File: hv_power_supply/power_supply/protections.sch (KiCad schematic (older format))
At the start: 7 parts, among them J1 MicroFit_RA_R_2, K1 DBR71210(NC), K2 LI12-1A85(NO), Q2 SSM3K333R, SW1 SW_Push_SPST_NO

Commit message: Remove resistor
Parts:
- removed J1: MicroFit_RA_R_2, footprints:MicroFit_RA_2, symbol formula:MicroFit_RA_R_2
- removed R2: R_100K, footprints:R_0805_OEM, symbol formula:R_100K
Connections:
- net labels removed: ACH+, ACH-
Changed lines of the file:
@@
 Wire Notes Line
 	3000 800  3000 2400
-$Comp
-L formula:MicroFit_RA_R_2 J1
-U 1 1 5FC7105C
-P 6400 1150
-F 0 "J1" H 6458 1425 50  0000 C CNN
-F 1 "MicroFit_RA_R_2" H 6458 1334 50  0000 C CNN
-F 2 "footprints:MicroFit_RA_2" H 6350 1350 50  0001 C CNN
-F 3 "https://www.molex.com/pdm_docs/sd/436500201_sd.pdf" H 6350 1350 50  0001 C CNN
-F 4 "DK" H 6500 1400 50  0001 C CNN "MFN"
-F 5 "WM1865-ND" H 6600 1500 50  0001 C CNN "MPN"
-F 6 "https://www.digikey.com/product-detail/en/molex/0436500201/WM1865-ND/268994" H 6400 1300 50  0001 C CNN "PurchasingLink"
-	1    6400 1150
-	1    0    0    -1
-$EndComp
-Text HLabel 6650 1100 2    47   Input ~ 0
-ACH+
-Text HLabel 6650 1200 2    47   Output ~ 0
-ACH-
 Wire Wire Line
 	800  1550 1300 1550
@@
 Wire Notes Line
 	600  2400 2650 2400
-$Comp
-L formula:R_100K R2
-U 1 1 5FC80149
-P 2050 1900
-F 0 "R2" H 2120 1946 50  0000 L CNN
-F 1 "R_100K" H 2120 1855 50  0000 L CNN
-F 2 "footprints:R_0805_OEM" H 1980 1900 50  0001 C CNN
-F 3 "https://industrial.panasonic.com/cdbs/www-data/pdf/RDA0000/AOA0000C304.pdf" H 2130 1900 50  0001 C CNN
-F 4 "DK" H 2050 1900 60  0001 C CNN "MFN"
-F 5 "P100KCCT-ND" H 2050 1900 60  0001 C CNN "MPN"
-F 6 "https://www.digikey.com/product-detail/en/panasonic-electronic-components/ERJ-6ENF1003V/P100KCCT-ND/119551" H 2530 2300 60  0001 C CNN "PurchasingLink"
-	1    2050 1900
-	1    0    0    -1
-$EndComp
 $EndSCHEMATC

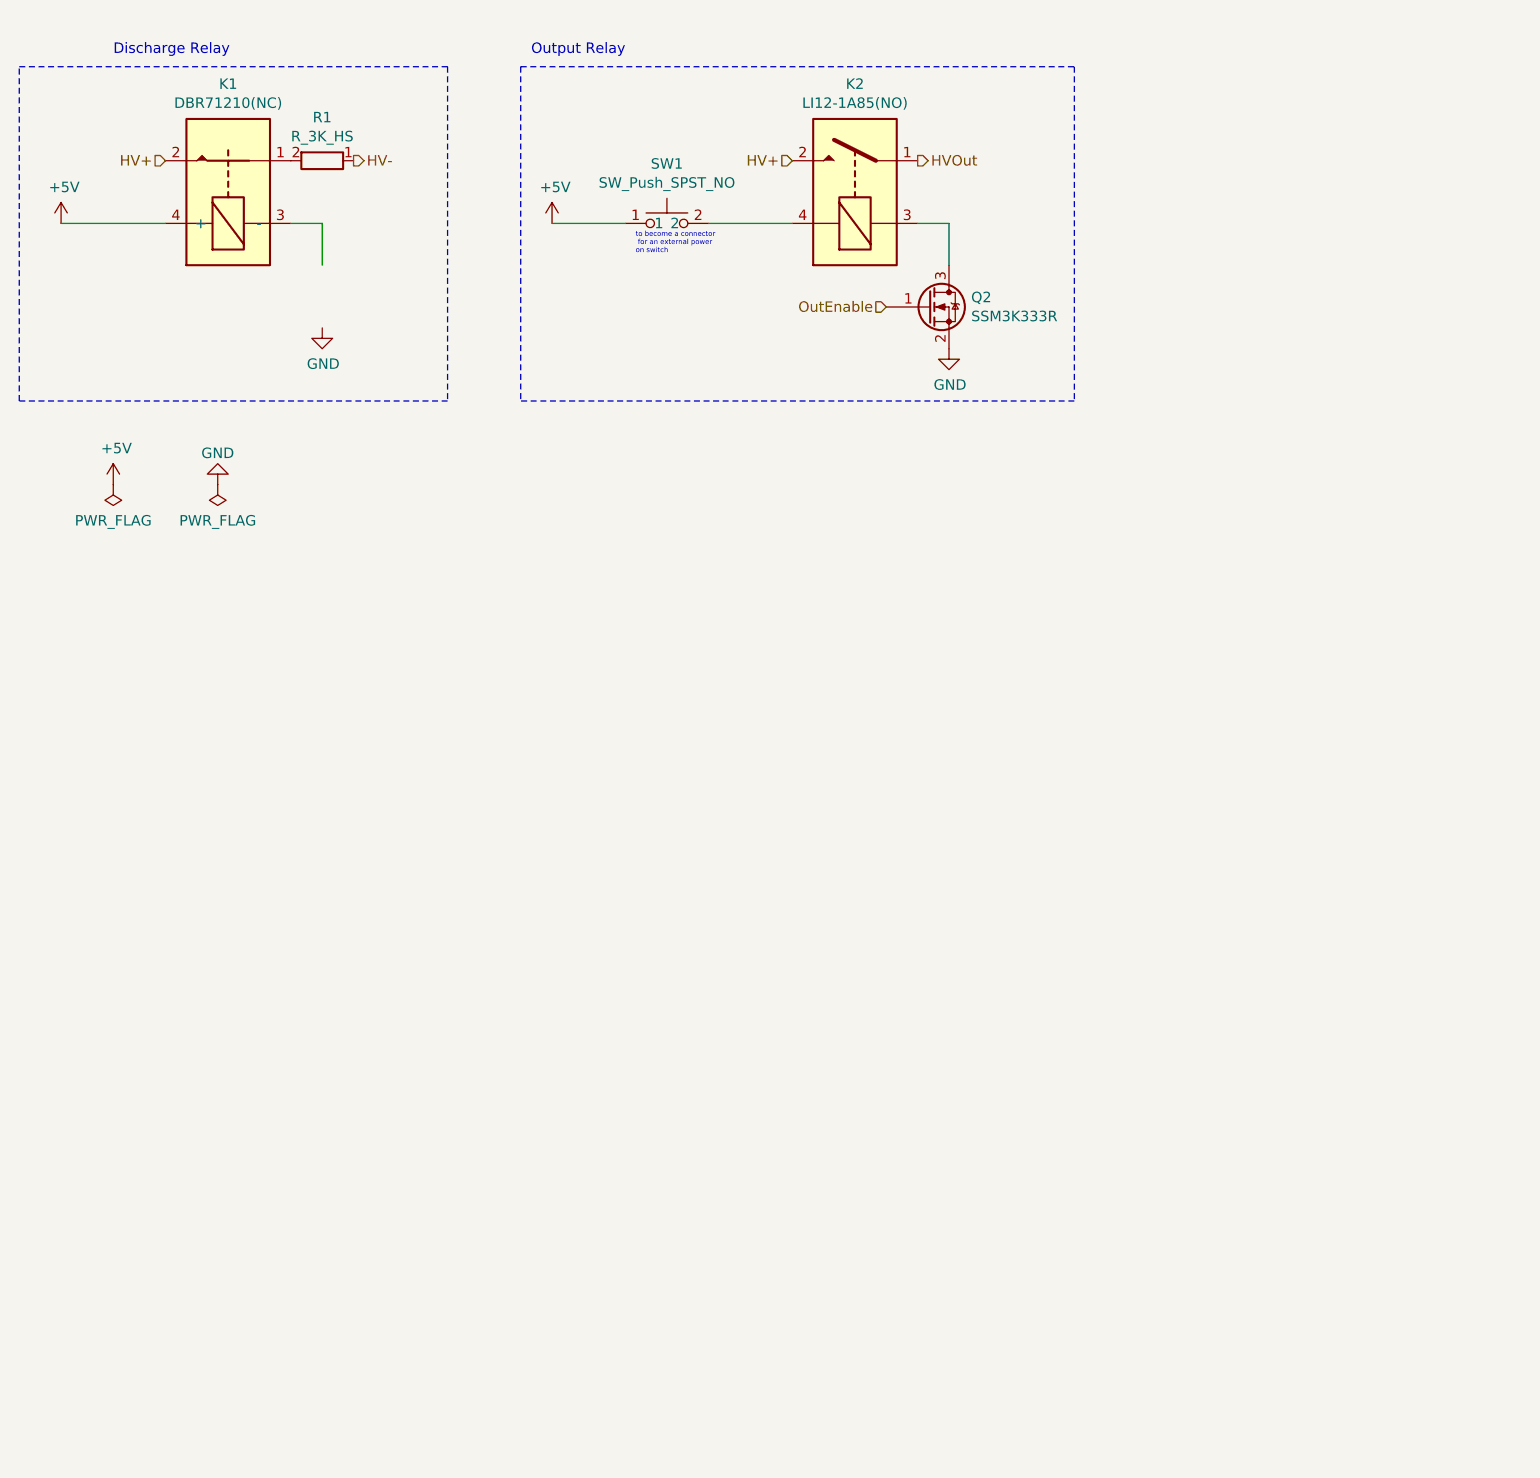
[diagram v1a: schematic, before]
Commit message: Add suppression diodes
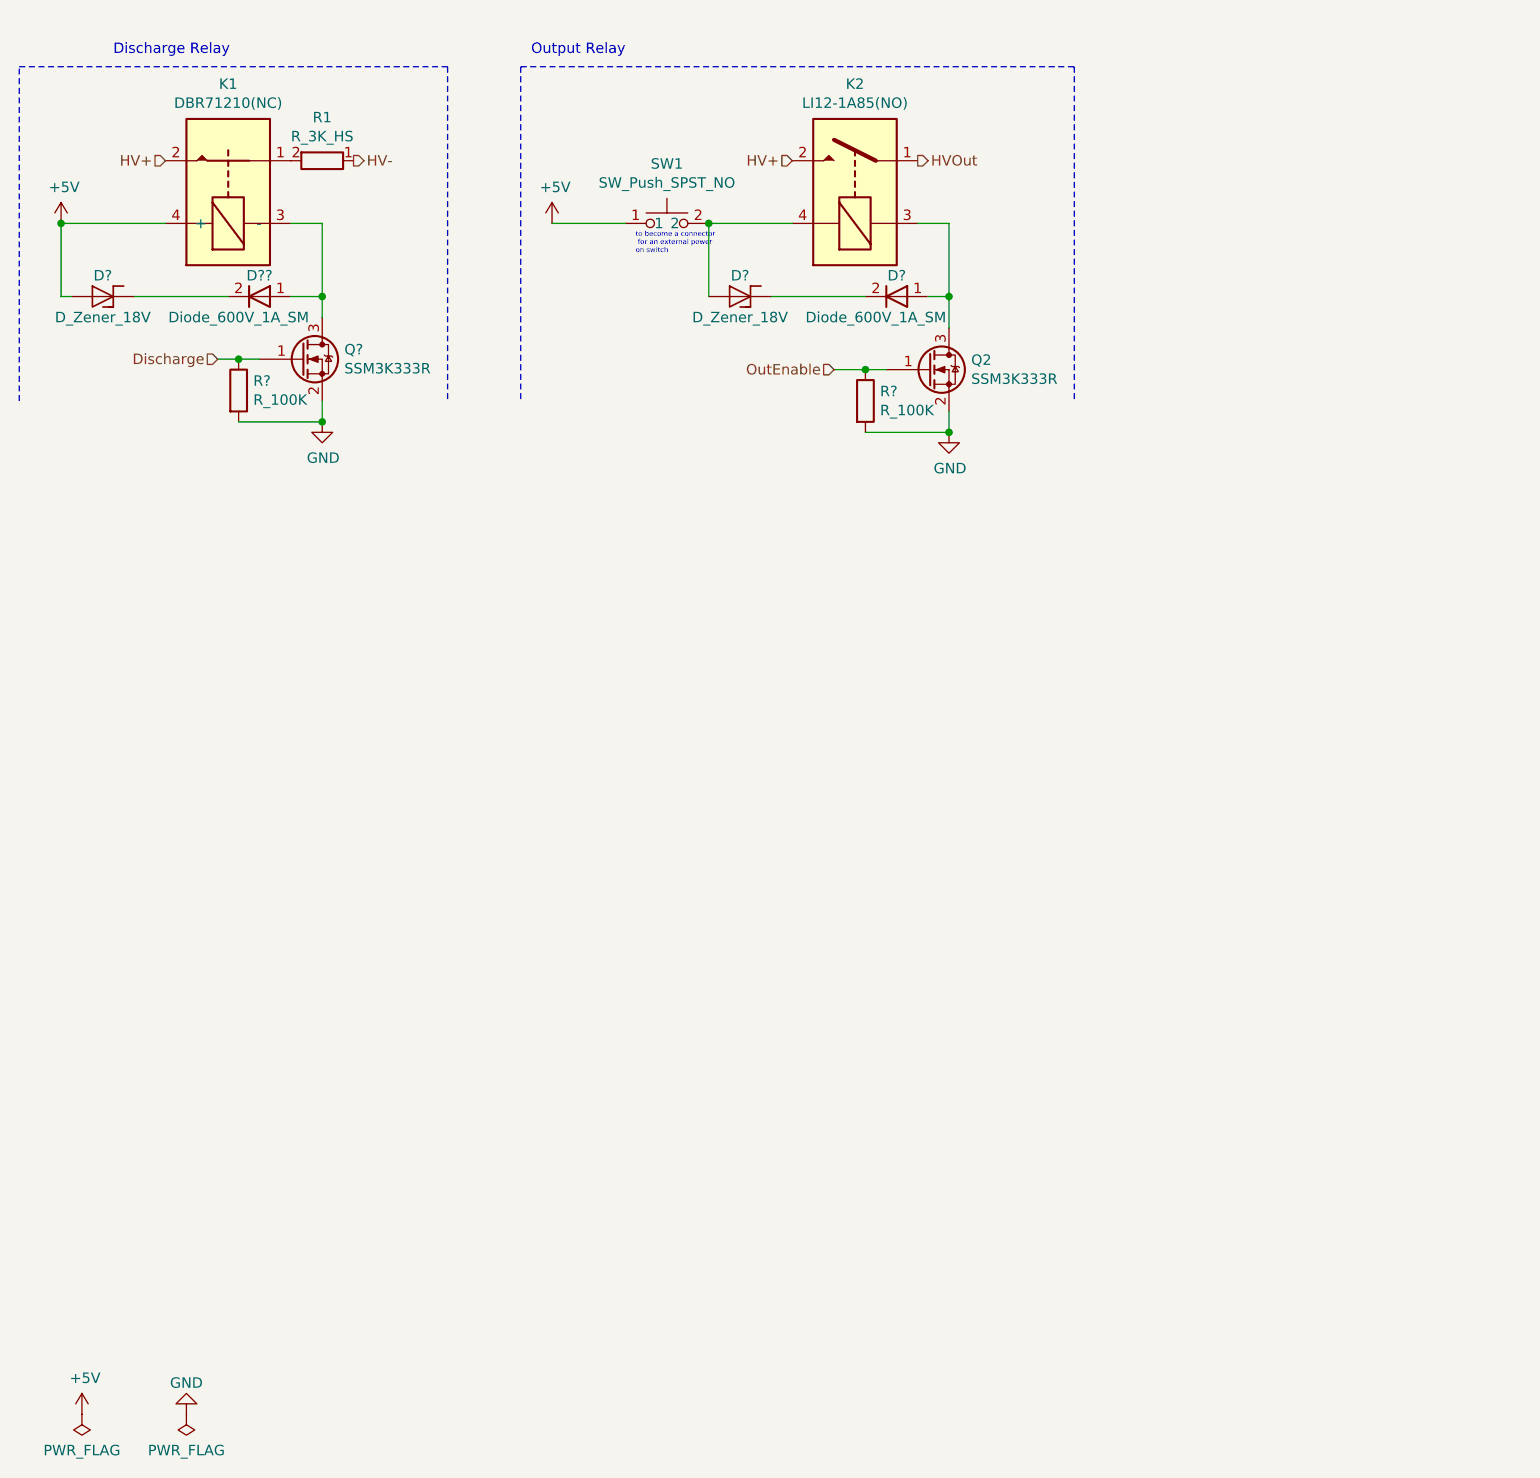
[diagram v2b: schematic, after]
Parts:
- added D? (x2): D_Zener_18V, footprints:DO-214AA, symbol formula:D_Zener_18V
- added D?, D??: Diode_600V_1A_SM, footprints:Diode_600V_1A_SM, symbol formula:Diode_600V_1A_SM
- added Q?: SSM3K333R, footprints:SOT-23F, symbol formula:SSM3K333R
- added R? (x2): R_100K, footprints:R_0805_OEM, symbol formula:R_100K
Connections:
- net labels added: Discharge
- wire segments 7 -> 24
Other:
- moved on the sheet: Q2
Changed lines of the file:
@@
 Wire Wire Line
 	1900 1550 2050 1550
-Wire Wire Line
-	2050 1550 2050 1750
 $Comp
 L power:GND #PWR04
 U 1 1 5FC34A9E
-P 2050 2050
-F 0 "#PWR04" H 2050 1800 50  0001 C CNN
-F 1 "GND" H 2055 1877 50  0000 C CNN
-F 2 "" H 2050 2050 50  0001 C CNN
-F 3 "" H 2050 2050 50  0001 C CNN
-	1    2050 2050
+P 2050 2500
+F 0 "#PWR04" H 2050 2250 50  0001 C CNN
+F 1 "GND" H 2055 2327 50  0000 C CNN
+F 2 "" H 2050 2500 50  0001 C CNN
+F 3 "" H 2050 2500 50  0001 C CNN
+	1    2050 2500
 	1    0    0    -1
 $EndComp
@@
 L power:+5V #PWR01
 U 1 1 5FC37E55
-P 1050 2800
-F 0 "#PWR01" H 1050 2650 50  0001 C CNN
-F 1 "+5V" H 1065 2973 50  0000 C CNN
-F 2 "" H 1050 2800 50  0001 C CNN
-F 3 "" H 1050 2800 50  0001 C CNN
-	1    1050 2800
+P 900 7250
+F 0 "#PWR01" H 900 7100 50  0001 C CNN
+F 1 "+5V" H 915 7423 50  0000 C CNN
+F 2 "" H 900 7250 50  0001 C CNN
+F 3 "" H 900 7250 50  0001 C CNN
+	1    900  7250
 	1    0    0    -1
 $EndComp
@@
 L power:PWR_FLAG #FLG01
 U 1 1 5FC38367
-P 1050 2800
-F 0 "#FLG01" H 1050 2875 50  0001 C CNN
-F 1 "PWR_FLAG" H 1050 2973 50  0000 C CNN
-F 2 "" H 1050 2800 50  0001 C CNN
-F 3 "~" H 1050 2800 50  0001 C CNN
-	1    1050 2800
+P 900 7250
+F 0 "#FLG01" H 900 7325 50  0001 C CNN
+F 1 "PWR_FLAG" H 900 7423 50  0000 C CNN
+F 2 "" H 900 7250 50  0001 C CNN
+F 3 "~" H 900 7250 50  0001 C CNN
+	1    900  7250
 	-1   0    0    1
 $EndComp
@@
 L power:PWR_FLAG #FLG02
 U 1 1 5FC38703
-P 1550 2800
-F 0 "#FLG02" H 1550 2875 50  0001 C CNN
-F 1 "PWR_FLAG" H 1550 2973 50  0000 C CNN
-F 2 "" H 1550 2800 50  0001 C CNN
-F 3 "~" H 1550 2800 50  0001 C CNN
-	1    1550 2800
+P 1400 7250
+F 0 "#FLG02" H 1400 7325 50  0001 C CNN
+F 1 "PWR_FLAG" H 1400 7423 50  0000 C CNN
+F 2 "" H 1400 7250 50  0001 C CNN
+F 3 "~" H 1400 7250 50  0001 C CNN
+	1    1400 7250
 	-1   0    0    1
 $EndComp
@@
 L power:GND #PWR02
 U 1 1 5FC38C25
-P 1550 2800
-F 0 "#PWR02" H 1550 2550 50  0001 C CNN
-F 1 "GND" H 1550 2650 50  0000 C CNN
-F 2 "" H 1550 2800 50  0001 C CNN
-F 3 "" H 1550 2800 50  0001 C CNN
-	1    1550 2800
+P 1400 7250
+F 0 "#PWR02" H 1400 7000 50  0001 C CNN
+F 1 "GND" H 1400 7100 50  0000 C CNN
+F 2 "" H 1400 7250 50  0001 C CNN
+F 3 "" H 1400 7250 50  0001 C CNN
+	1    1400 7250
 	-1   0    0    1
 $EndComp
@@
 L formula:SSM3K333R Q2
 U 1 1 5FC3EB17
-P 4950 1950
-F 0 "Q2" H 5156 1996 50  0000 L CNN
-F 1 "SSM3K333R" H 5156 1905 50  0000 L CNN
-F 2 "footprints:SOT-23F" H 5150 1875 50  0001 L CIN
-F 3 "https://drive.google.com/drive/folders/0B-V-iZf33Y4GNzhDQTJZanJRbVk" H 5150 2025 50  0001 L CNN
-F 4 "DK" H 5450 2325 60  0001 C CNN "MFN"
-F 5 "SSM3K333RLFCT-ND" H 5350 2225 60  0001 C CNN "MPN"
-F 6 "https://www.digikey.com/product-detail/en/toshiba-semiconductor-and-storage/SSM3K333RLF/SSM3K333RLFCT-ND/3522391" H 5250 2125 60  0001 C CNN "PurchasingLink"
-	1    4950 1950
+P 4950 2250
+F 0 "Q2" H 5156 2296 50  0000 L CNN
+F 1 "SSM3K333R" H 5156 2205 50  0000 L CNN
+F 2 "footprints:SOT-23F" H 5150 2175 50  0001 L CIN
+F 3 "https://drive.google.com/drive/folders/0B-V-iZf33Y4GNzhDQTJZanJRbVk" H 5150 2325 50  0001 L CNN
+F 4 "DK" H 5450 2625 60  0001 C CNN "MFN"
+F 5 "SSM3K333RLFCT-ND" H 5350 2525 60  0001 C CNN "MPN"
+F 6 "https://www.digikey.com/product-detail/en/toshiba-semiconductor-and-storage/SSM3K333RLF/SSM3K333RLFCT-ND/3522391" H 5250 2425 60  0001 C CNN "PurchasingLink"
+	1    4950 2250
 	1    0    0    -1
 $EndComp
@@
 	1    0    0    -1
 $EndComp
-Text HLabel 4750 1950 0    50   Input ~ 0
+Text HLabel 4500 2250 0    50   Input ~ 0
 OutEnable
 $Comp
@@
 HV+
 Wire Wire Line
-	5050 1750 5050 1550
-Wire Wire Line
 	5050 1550 4900 1550
 $Comp
 L power:GND #PWR06
 U 1 1 5FC4F4BB
-P 5050 2150
-F 0 "#PWR06" H 5050 1900 50  0001 C CNN
-F 1 "GND" H 5055 1977 50  0000 C CNN
-F 2 "" H 5050 2150 50  0001 C CNN
-F 3 "" H 5050 2150 50  0001 C CNN
-	1    5050 2150
+P 5050 2550
+F 0 "#PWR06" H 5050 2300 50  0001 C CNN
+F 1 "GND" H 5055 2377 50  0000 C CNN
+F 2 "" H 5050 2550 50  0001 C CNN
+F 3 "" H 5050 2550 50  0001 C CNN
+	1    5050 2550
 	1    0    0    -1
 $EndComp
@@
 Wire Notes Line
 	3000 800  5650 800
-Wire Notes Line
-	5650 2400 3000 2400
 Text Notes 3050 750  0    50   ~ 0
 Output Relay
@@
 Wire Notes Line
 	600  800  2650 800
-Wire Notes Line
-	600  2400 2650 2400
+$Comp
+L formula:Diode_600V_1A_SM D??
+U 1 1 5FC85209
+P 1750 1900
+F 0 "D??" H 1750 1800 50  0000 C CNN
+F 1 "Diode_600V_1A_SM" H 1850 2000 50  0000 C CNN
+F 2 "footprints:Diode_600V_1A_SM" H 1700 2050 50  0001 C CNN
+F 3 "https://www.st.com/content/ccc/resource/technical/document/datasheet/c7/d5/fe/c4/56/21/41/02/CD00005135.pdf/files/CD00005135.pdf/jcr:content/translations/en.CD00005135.pdf" H 1700 2050 50  0001 C CNN
+F 4 "https://www.digikey.com/product-detail/en/stmicroelectronics/STTH1R06A/497-3765-1-ND/691935" H 1750 2100 50  0001 C CNN "Purchasing Link"
+	1    1750 1900
+	-1   0    0    1
+$EndComp
+$Comp
+L formula:D_Zener_18V D?
+U 1 1 5FC870AF
+P 1000 1900
+F 0 "D?" H 1000 1800 50  0000 C CNN
+F 1 "D_Zener_18V" H 1000 2000 50  0000 C CNN
+F 2 "footprints:DO-214AA" H 900 1900 50  0001 C CNN
+F 3 "http://www.mccsemi.com/up_pdf/SMBJ5338B-SMBJ5388B(SMB).pdf" H 1000 2000 50  0001 C CNN
+F 4 "DK" H 1200 2200 60  0001 C CNN "MFN"
+F 5 "SMBJ5355B-TPMSCT-ND" H 1100 2100 60  0001 C CNN "MPN"
+F 6 "https://www.digikey.com/products/en?keywords=SMBJ5355B-TPMSCT-ND" H 1400 2400 60  0001 C CNN "PurchasingLink"
+	1    1000 1900
+	-1   0    0    1
+$EndComp
+Wire Wire Line
+	1900 1900 2050 1900
+Wire Wire Line
+	2050 1550 2050 1900
+Wire Wire Line
+	800  1900 800  1550
+Connection ~ 800  1550
+$Comp
+L formula:SSM3K333R Q?
+U 1 1 5FC8A045
+P 1950 2200
+F 0 "Q?" H 2156 2246 50  0000 L CNN
+F 1 "SSM3K333R" H 2156 2155 50  0000 L CNN
+F 2 "footprints:SOT-23F" H 2150 2125 50  0001 L CIN
+F 3 "https://drive.google.com/drive/folders/0B-V-iZf33Y4GNzhDQTJZanJRbVk" H 2150 2275 50  0001 L CNN
+F 4 "DK" H 2450 2575 60  0001 C CNN "MFN"
+F 5 "SSM3K333RLFCT-ND" H 2350 2475 60  0001 C CNN "MPN"
+F 6 "https://www.digikey.com/product-detail/en/toshiba-semiconductor-and-storage/SSM3K333RLF/SSM3K333RLFCT-ND/3522391" H 2250 2375 60  0001 C CNN "PurchasingLink"
+	1    1950 2200
+	1    0    0    -1
+$EndComp
+Wire Wire Line
+	4500 2250 4650 2250
+$Comp
+L formula:R_100K R?
+U 1 1 5FC905D7
+P 4650 2400
+F 0 "R?" H 4720 2446 50  0000 L CNN
+F 1 "R_100K" H 4720 2355 50  0000 L CNN
+F 2 "footprints:R_0805_OEM" H 4580 2400 50  0001 C CNN
+F 3 "https://industrial.panasonic.com/cdbs/www-data/pdf/RDA0000/AOA0000C304.pdf" H 4730 2400 50  0001 C CNN
+F 4 "DK" H 4650 2400 60  0001 C CNN "MFN"
+F 5 "P100KCCT-ND" H 4650 2400 60  0001 C CNN "MPN"
+F 6 "https://www.digikey.com/product-detail/en/panasonic-electronic-components/ERJ-6ENF1003V/P100KCCT-ND/119551" H 5130 2800 60  0001 C CNN "PurchasingLink"
+	1    4650 2400
+	1    0    0    -1
+$EndComp
+Connection ~ 4650 2250
+Wire Wire Line
+	4650 2250 4750 2250
+Wire Wire Line
+	4650 2550 5050 2550
+Wire Wire Line
+	5050 2450 5050 2550
+Connection ~ 5050 2550
+$Comp
+L formula:R_100K R?
+U 1 1 5FC97986
+P 1650 2350
+F 0 "R?" H 1720 2396 50  0000 L CNN
+F 1 "R_100K" H 1720 2305 50  0000 L CNN
+F 2 "footprints:R_0805_OEM" H 1580 2350 50  0001 C CNN
+F 3 "https://industrial.panasonic.com/cdbs/www-data/pdf/RDA0000/AOA0000C304.pdf" H 1730 2350 50  0001 C CNN
+F 4 "DK" H 1650 2350 60  0001 C CNN "MFN"
+F 5 "P100KCCT-ND" H 1650 2350 60  0001 C CNN "MPN"
+F 6 "https://www.digikey.com/product-detail/en/panasonic-electronic-components/ERJ-6ENF1003V/P100KCCT-ND/119551" H 2130 2750 60  0001 C CNN "PurchasingLink"
+	1    1650 2350
+	1    0    0    -1
+$EndComp
+Text HLabel 1550 2200 0    50   Input ~ 0
+Discharge
+Wire Wire Line
+	1650 2200 1750 2200
+Wire Wire Line
+	1650 2500 2050 2500
+Wire Wire Line
+	2050 2400 2050 2500
+Connection ~ 2050 2500
+Wire Wire Line
+	850  1900 800  1900
+Wire Wire Line
+	1150 1900 1600 1900
+Wire Wire Line
+	2050 1900 2050 2000
+Connection ~ 2050 1900
+$Comp
+L formula:D_Zener_18V D?
+U 1 1 5FCA7EE2
+P 4050 1900
+F 0 "D?" H 4050 1800 50  0000 C CNN
+F 1 "D_Zener_18V" H 4050 2000 50  0000 C CNN
+F 2 "footprints:DO-214AA" H 3950 1900 50  0001 C CNN
+F 3 "http://www.mccsemi.com/up_pdf/SMBJ5338B-SMBJ5388B(SMB).pdf" H 4050 2000 50  0001 C CNN
+F 4 "DK" H 4250 2200 60  0001 C CNN "MFN"
+F 5 "SMBJ5355B-TPMSCT-ND" H 4150 2100 60  0001 C CNN "MPN"
+F 6 "https://www.digikey.com/products/en?keywords=SMBJ5355B-TPMSCT-ND" H 4450 2400 60  0001 C CNN "PurchasingLink"
+	1    4050 1900
+	-1   0    0    1
+$EndComp
+$Comp
+L formula:Diode_600V_1A_SM D?
+U 1 1 5FCADFFB
+P 4800 1900
+F 0 "D?" H 4800 1800 50  0000 C CNN
+F 1 "Diode_600V_1A_SM" H 4900 2000 50  0000 C CNN
+F 2 "footprints:Diode_600V_1A_SM" H 4750 2050 50  0001 C CNN
+F 3 "https://www.st.com/content/ccc/resource/technical/document/datasheet/c7/d5/fe/c4/56/21/41/02/CD00005135.pdf/files/CD00005135.pdf/jcr:content/translations/en.CD00005135.pdf" H 4750 2050 50  0001 C CNN
+F 4 "https://www.digikey.com/product-detail/en/stmicroelectronics/STTH1R06A/497-3765-1-ND/691935" H 4800 2100 50  0001 C CNN "Purchasing Link"
+	1    4800 1900
+	-1   0    0    1
+$EndComp
+Wire Wire Line
+	4200 1900 4650 1900
+Wire Wire Line
+	5050 1550 5050 1900
+Wire Wire Line
+	4950 1900 5050 1900
+Connection ~ 5050 1900
+Wire Wire Line
+	5050 1900 5050 2050
+Wire Wire Line
+	3900 1900 3900 1550
+Connection ~ 3900 1550
+Wire Wire Line
+	1650 2200 1550 2200
+Connection ~ 1650 2200
 $EndSCHEMATC
